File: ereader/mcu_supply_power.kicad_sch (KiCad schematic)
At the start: 26 parts, among them U1 R7KA8P1KFLCAC#UC0, U23 LT3042IMSE#PBF

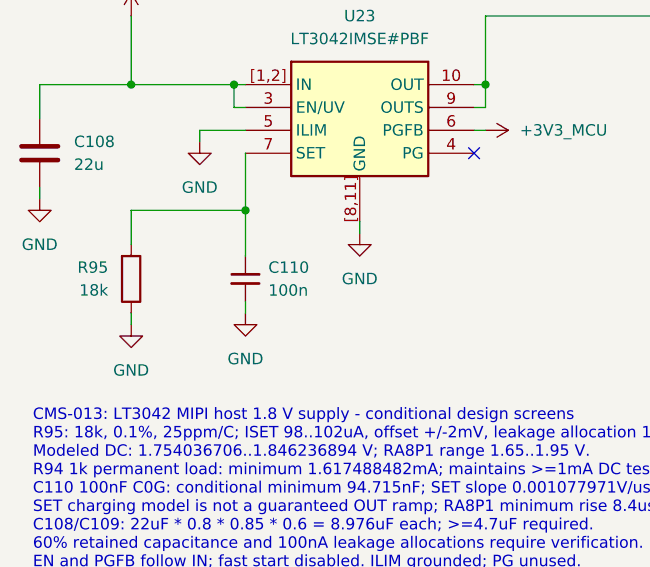
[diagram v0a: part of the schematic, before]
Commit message: WIP: integrate orientation sensor and refresh schematic review exports
Add LIS2DW12 host wiring and sourced passives, revise held-supply discharge calculations, document camera and capacitance screens, and refresh standard capacitor caches. Include reviewed 14-page PDF and reconciled native BOM. ERC remains 111 errors and 11 warnings; electrical design is incomplete. Refs #21.
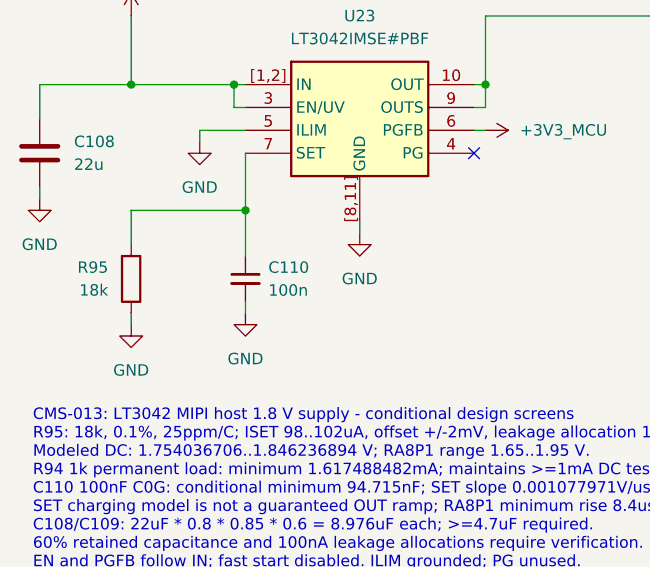
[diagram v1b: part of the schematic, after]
